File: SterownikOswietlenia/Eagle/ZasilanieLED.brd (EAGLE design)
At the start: 68 x 45 mm, 24 parts, among them Q1 SPD30P06PTO252, Q2 SPD30P06PTO252, Q3 SPD30P06PTO252, T1 BC847, T2 BC847, T3 BC847, U1 WS2801, X1 5569-02, X2 5569-02, X3 5569-02, X4 5569-08, X5 5569-08

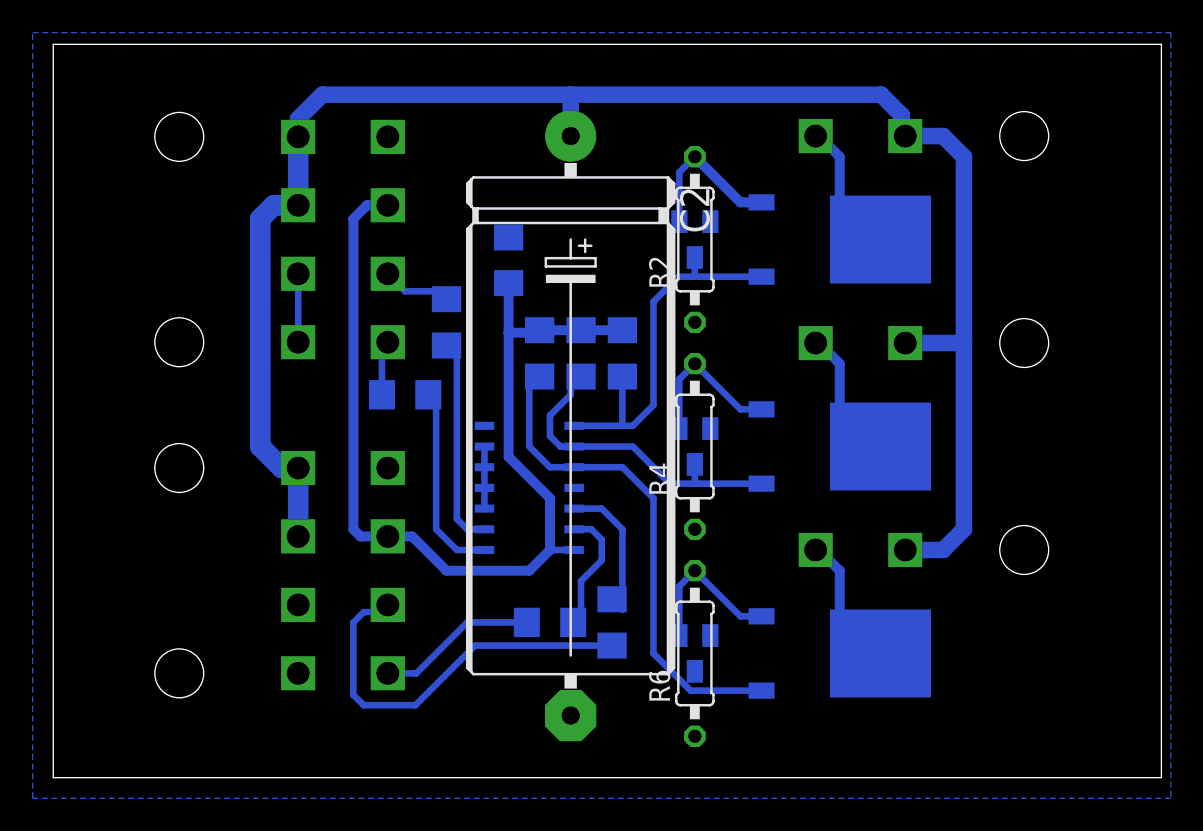
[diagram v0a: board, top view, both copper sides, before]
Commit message: uporzą▲dkowane opisy elementów
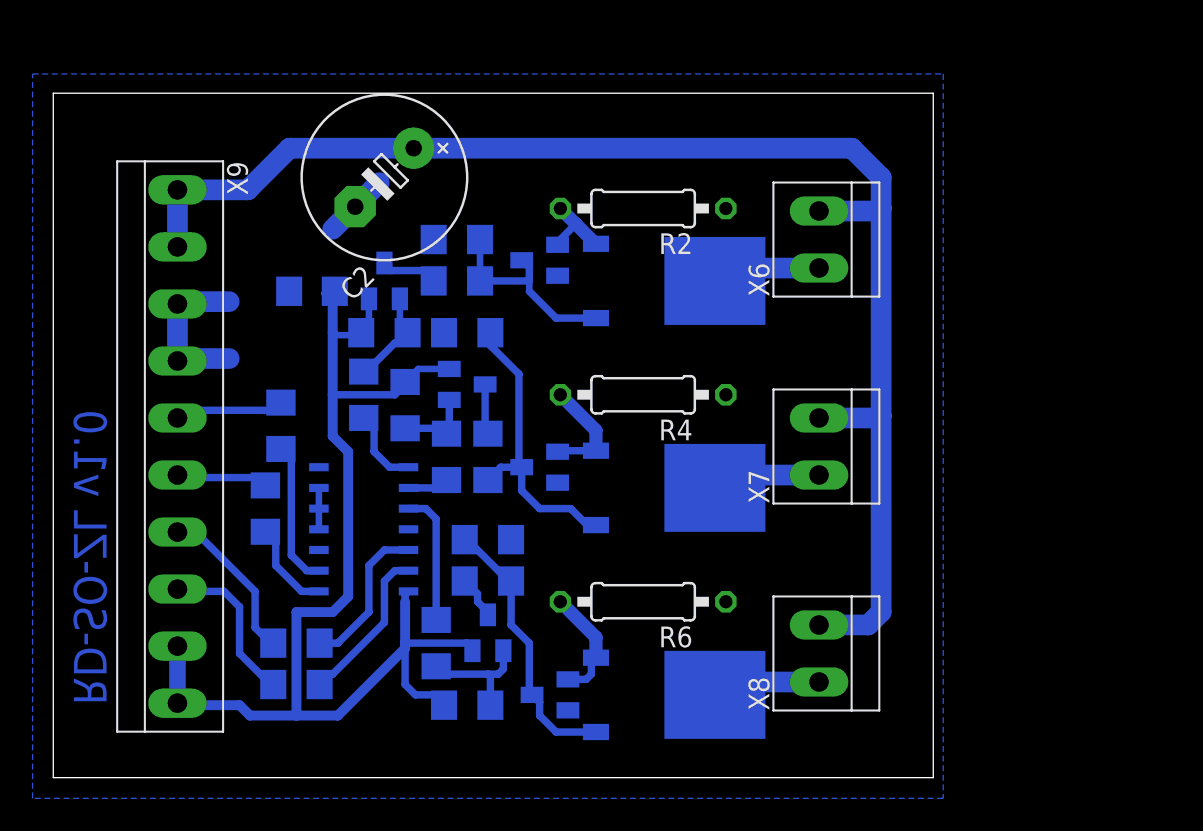
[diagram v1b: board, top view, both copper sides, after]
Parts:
- removed X1, X2, X3: 5569-02, con-molex-5569:5569-02
- removed X4, X5: 5569-08, con-molex-5569:5569-08
- added R11, R12, R13, R17, R18, R19: 1k, rcl:R1206
- added R14, R15, R16: 3k3, rcl:R1206
- added T4, T5, T6: BC857, transistor:SOT23-BEC
- added X6, X7, X8: (no value), con-ria-59:2POL35
- added X9: (no value), con-ria-59:10POL35
- C2: device rcl:E35-12 -> rcl:E5-10,5
- Q1, Q2, Q3: value SPD30P06PTO252 -> NMOS
- moved R10 19.4 mm to (14.9, 8.26), turned to 0 degrees
- moved C2 19.0 mm to (20.3, 36.8), turned to 225 degrees
- moved R9 16.0 mm to (14.9, 5.71)
- moved R5 14.3 mm to (26.7, 12.1), turned to 0 degrees
- moved C1 12.2 mm to (15.9, 29.8), turned to 0 degrees
- moved R8 12.0 mm to (14.0, 21.6)
- moved R1 11.1 mm to (24.8, 30.5), turned to 0 degrees
- moved R7 11.1 mm to (13.0, 16.5), turned to 270 degrees
- moved U1 10.5 mm to (19.1, 15.2)
- moved Q1 10.5 mm to (38.1, 30.5)
- moved Q2 10.5 mm to (38.1, 17.8)
- moved Q3 10.5 mm to (38.1, 5.08)
- moved T1 9.61 mm to (29.8, 31.8), turned to 270 degrees
- moved T2 9.61 mm to (29.8, 19.1), turned to 270 degrees
- moved T3 9.25 mm to (30.5, 5.08), turned to 270 degrees
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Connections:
- new net N$14: R1.2, T4.C
- new net N$15: R3.2, T5.C
- new net N$16: R5.2, T6.C
- new net N$17: Q1.1, R1.1, R11.2, T1.3
- new net N$18: Q2.1, R12.2, R3.1, T2.3
- new net N$19: Q3.1, R13.2, R5.1, T3.3
- new net N$20: R14.2, R17.1, T4.B
- new net N$21: R15.2, R18.1, T5.B
- new net N$22: R16.2, R19.1, T6.B
- net +24V: now also X6.2, X7.2, X8.2, X9.1, X9.2; no longer X1.1, X2.1, X3.1, X4.3, X4.4, X5.3, X5.4
- net CKI: now also X9.6; no longer X4.5
- net CKO: now also X9.8; no longer X5.5
- net GND: now also R11.1, R12.1, R13.1, X9.3, X9.4; no longer U1.3, X4.1, X4.2, X5.1, X5.2
- net N$11: now also X6.1; no longer X1.2
- net N$12: now also X7.1; no longer X2.2
- net N$13: now also X8.1; no longer X3.2
- net N$4: now also R14.1; no longer Q1.1, R1.1, T1.3
- net N$5: now also R15.1; no longer Q2.1, R3.1, T2.3
- net N$6: now also R16.1; no longer Q3.1, R5.1, T3.3
- net SDI: now also X9.5; no longer X4.6
- net SDO: now also X9.7; no longer X5.6
- net VCC: now also R17.2, R18.2, R19.2, T4.E, T5.E, T6.E, X9.10, X9.9; no longer R1.2, R3.2, R5.2, X4.7, X5.7
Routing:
- net N$6: track 30.6 -> 8.16 mm
- net +24V: track 105.8 -> 87.0 mm
- net N$4: track 23.2 -> 4.84 mm
- net N$18: track 0.00 -> 18.3 mm
- net N$5: track 19.8 -> 2.68 mm
- net N$19: track 0.00 -> 16.8 mm
- net SDO: track 24.7 -> 10.0 mm
- net VCC: track 61.1 -> 74.6 mm
- net N$17: track 0.00 -> 12.4 mm
- net GND: track 8.01 -> 16.7 mm
- net N$22: track 0.00 -> 7.55 mm
- net N$1: track 11.9 -> 5.73 mm
- net N$20: track 0.00 -> 6.05 mm
- net N$21: track 0.00 -> 4.92 mm
- net N$7: track 9.62 -> 4.82 mm
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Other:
- board size 68 x 45 mm -> 54 x 42 mm
- board text added: "RD-SO-ZL v1.0"
